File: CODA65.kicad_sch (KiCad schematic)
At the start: 32 parts, among them J1 Conn_01x04, J2 Conn_01x05, U1 RP2040, U2 W25Q128JVS, U3 XC6206PxxxMR, Y1 Crystal_GND24

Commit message: Routing Done
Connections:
- net ROW1: now reaches U1.11 (GPIO8)
- net COL14: now reaches U1.12 (GPIO9)
- net COL9: now reaches U1.13 (GPIO10)
- net ROW4: now reaches U1.14 (GPIO11)
- net COL6: now reaches U1.15 (GPIO12)
- net ROW0: now reaches U1.6 (GPIO4)
- net ROW3: now reaches U1.7 (GPIO5)
- net COL12: now reaches U1.8 (GPIO6)
- net ROW2: now reaches U1.9 (GPIO7)
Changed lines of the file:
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@@
+    )
+  )
+  (global_label "COL12" (shape input) (at 247.65 69.85 0) (fields_autoplaced)
+    (effects (font (size 1.27 1.27)) (justify left))
+    (property "Intersheetrefs" "${INTERSHEET_REFS}" (at 256.6828 69.85 0)
+      (effects (font (size 1.27 1.27)) (justify left) hide)
     )
   )
@@
     )
   )
+  (global_label "ROW1" (shape input) (at 247.65 74.93 0) (fields_autoplaced)
+    (effects (font (size 1.27 1.27)) (justify left))
+    (property "Intersheetrefs" "${INTERSHEET_REFS}" (at 255.8966 74.93 0)
+      (effects (font (size 1.27 1.27)) (justify left) hide)
+    )
+  )
   (global_label "XIN" (shape input) (at 167.64 105.41 0) (fields_autoplaced)
     (effects (font (size 1.27 1.27)) (justify left))
@@
     )
   )
+  (global_label "ROW4" (shape input) (at 247.65 82.55 0) (fields_autoplaced)
+    (effects (font (size 1.27 1.27)) (justify left))
+    (property "Intersheetrefs" "${INTERSHEET_REFS}" (at 255.8966 82.55 0)
+      (effects (font (size 1.27 1.27)) (justify left) hide)
+    )
+  )
   (global_label "RESET" (shape input) (at 196.85 54.61 180) (fields_autoplaced)
     (effects (font (size 1.27 1.27)) (justify right))
@@
     )
   )
+  (global_label "ROW3" (shape input) (at 247.65 67.31 0) (fields_autoplaced)
+    (effects (font (size 1.27 1.27)) (justify left))
+    (property "Intersheetrefs" "${INTERSHEET_REFS}" (at 255.8966 67.31 0)
+      (effects (font (size 1.27 1.27)) (justify left) hide)
+    )
+  )
   (global_label "Q_IO1" (shape input) (at 196.85 80.01 180) (fields_autoplaced)
     (effects (font (size 1.27 1.27)) (justify right))
@@
     )
   )
+  (global_label "COL14" (shape input) (at 247.65 77.47 0) (fields_autoplaced)
+    (effects (font (size 1.27 1.27)) (justify left))
+    (property "Intersheetrefs" "${INTERSHEET_REFS}" (at 256.6828 77.47 0)
+      (effects (font (size 1.27 1.27)) (justify left) hide)
+    )
+  )
   (global_label "XOUT" (shape input) (at 167.64 113.03 0) (fields_autoplaced)
     (effects (font (size 1.27 1.27)) (justify left))
@@
     )
   )
+  (global_label "ROW2" (shape input) (at 247.65 72.39 0) (fields_autoplaced)
+    (effects (font (size 1.27 1.27)) (justify left))
+    (property "Intersheetrefs" "${INTERSHEET_REFS}" (at 255.8966 72.39 0)
+      (effects (font (size 1.27 1.27)) (justify left) hide)
+    )
+  )
   (global_label "Q_IO2" (shape input) (at 196.85 82.55 180) (fields_autoplaced)
     (effects (font (size 1.27 1.27)) (justify right))
@@
     )
   )
+  (global_label "COL6" (shape input) (at 247.65 85.09 0) (fields_autoplaced)
+    (effects (font (size 1.27 1.27)) (justify left))
+    (property "Intersheetrefs" "${INTERSHEET_REFS}" (at 255.4733 85.09 0)
+      (effects (font (size 1.27 1.27)) (justify left) hide)
+    )
+  )
   (global_label "D-" (shape input) (at 182.88 66.04 180) (fields_autoplaced)
     (effects (font (size 1.27 1.27)) (justify right))
@@
     )
   )
+  (global_label "ROW0" (shape input) (at 247.65 64.77 0) (fields_autoplaced)
+    (effects (font (size 1.27 1.27)) (justify left))
+    (property "Intersheetrefs" "${INTERSHEET_REFS}" (at 255.8966 64.77 0)
+      (effects (font (size 1.27 1.27)) (justify left) hide)
+    )
+  )
   (global_label "COL7" (shape input) (at 247.65 59.69 0) (fields_autoplaced)
     (effects (font (size 1.27 1.27)) (justify left))
@@
       (effects (font (size 1.27 1.27)) (justify left) hide)
     )
+  )
+  (global_label "COL9" (shape input) (at 247.65 80.01 0) (fields_autoplaced)
+    (effects (font (size 1.27 1.27)) (justify left))
+    (property "Intersheetrefs" "${INTERSHEET_REFS}" (at 255.4733 80.01 0)
+      (effects (font (size 1.27 1.27)) (justify left) hide)
+    )

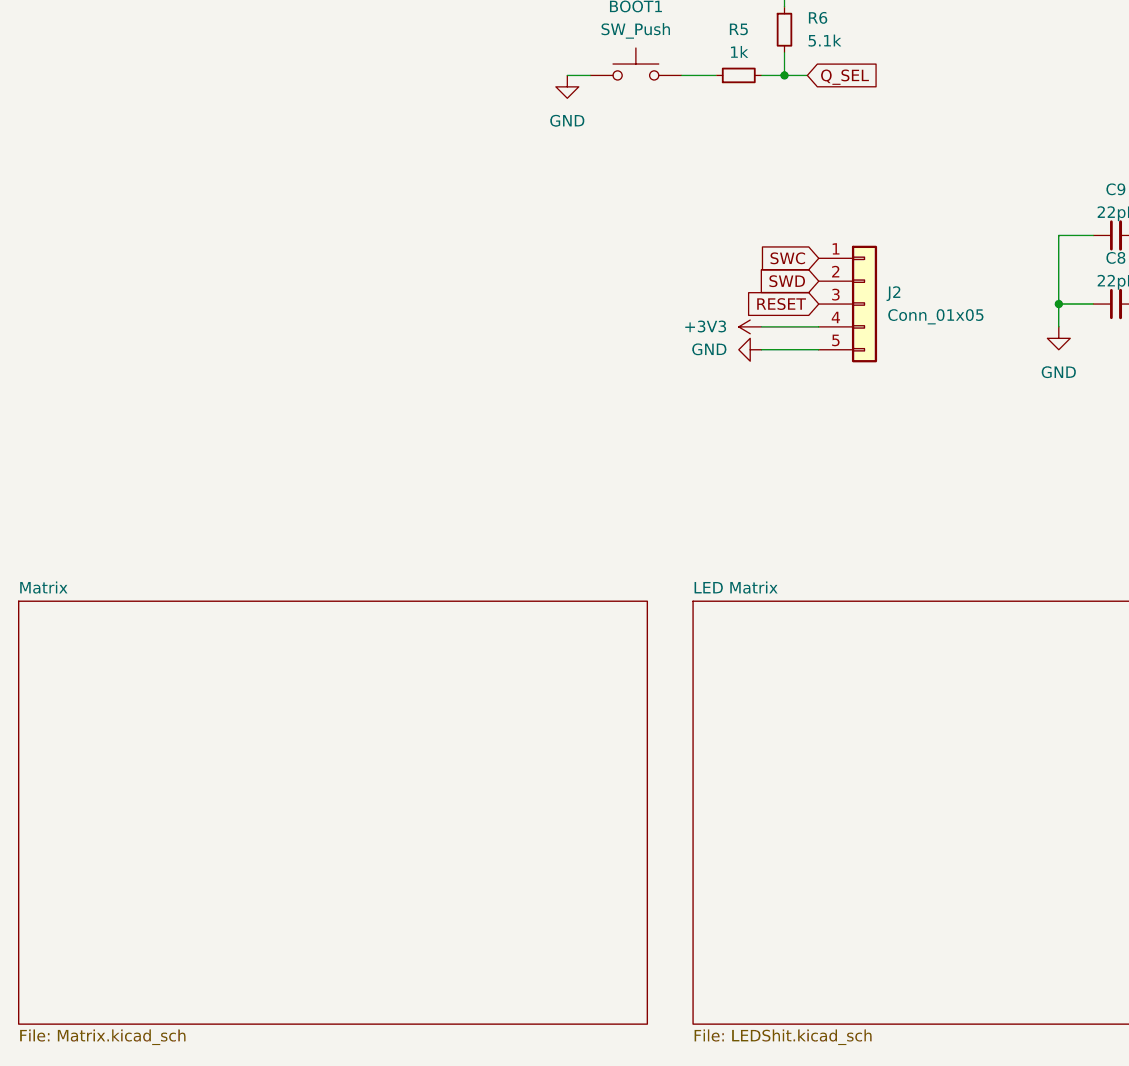
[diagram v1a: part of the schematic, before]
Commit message: Filename Changes
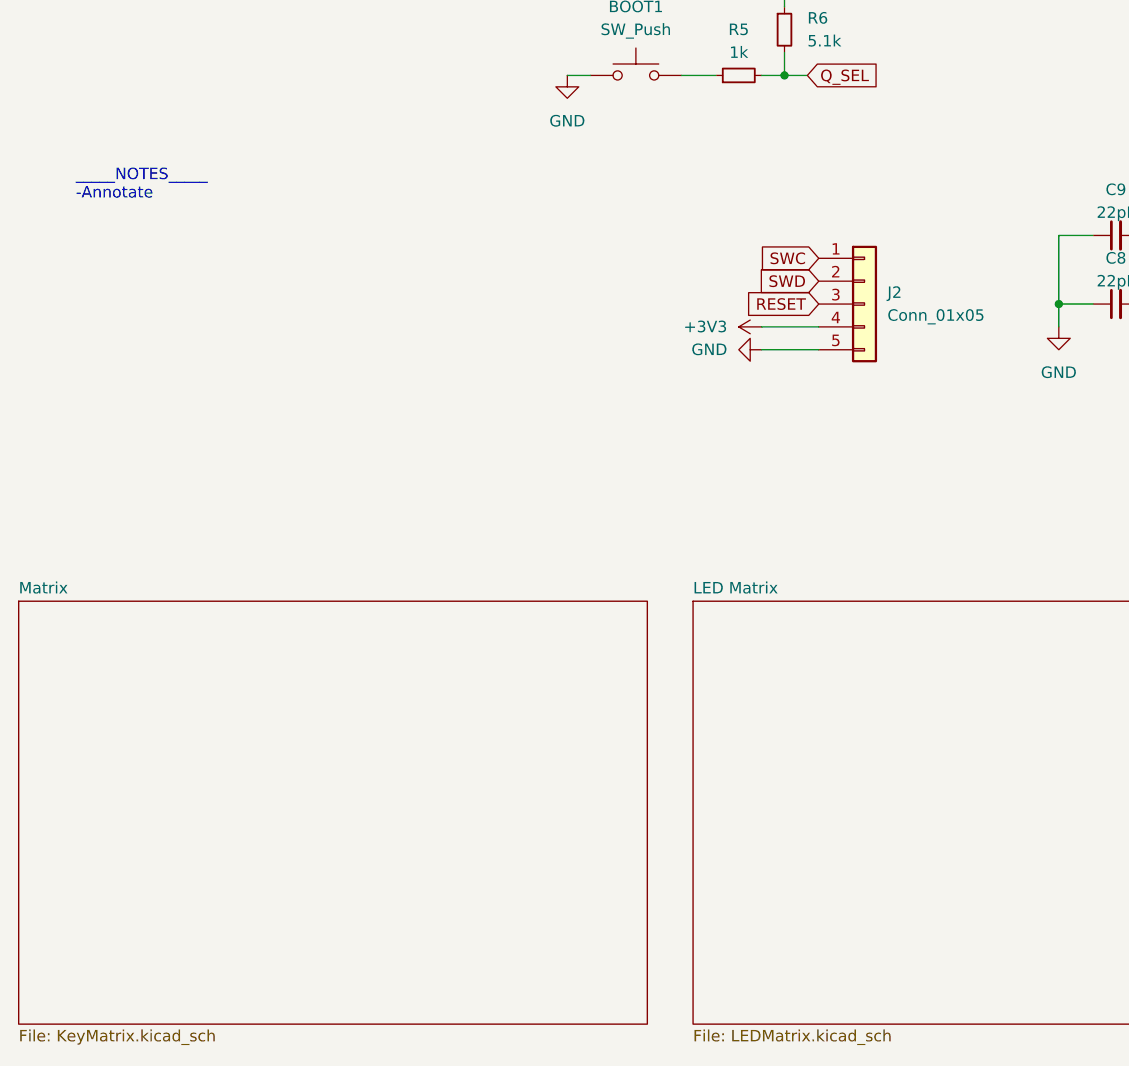
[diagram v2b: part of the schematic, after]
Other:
- sheet LED Matrix: file LEDShit.kicad_sch -> LEDMatrix.kicad_sch
- sheet Matrix: file Matrix.kicad_sch -> KeyMatrix.kicad_sch
- note added: "_____NOTES_____ -Annotate"
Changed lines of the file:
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@@
     (stroke (width 0) (type default))
+  )
+  (text "_____NOTES_____\n-Annotate " (at 20.32 101.6 0)
+    (effects (font (size 1.27 1.27)) (justify left bottom))
   )
   (global_label "Q_IO2" (shape input) (at 133.35 41.91 180) (fields_autoplaced)
@@
       (effects (font (size 1.27 1.27)) (justify left bottom))
     )
-    (property "Sheetfile" "LEDShit.kicad_sch" (at 88.9 193.6246 0)
+    (property "Sheetfile" "LEDMatrix.kicad_sch" (at 88.9 193.6246 0)
       (effects (font (size 1.27 1.27)) (justify left top))
     )
@@
       (effects (font (size 1.27 1.27)) (justify left bottom))
     )
-    (property "Sheetfile" "Matrix.kicad_sch" (at 13.97 193.6246 0)
+    (property "Sheetfile" "KeyMatrix.kicad_sch" (at 13.97 193.6246 0)
       (effects (font (size 1.27 1.27)) (justify left top))
     )
